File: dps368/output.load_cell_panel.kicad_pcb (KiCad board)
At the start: 2 copper layers, 50 x 46 mm, 167 parts, among them J1 Conn_01x05_Female, U1 DPS368XTSA1

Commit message: goddamn it
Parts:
- removed the ? at (141.1, 71.3)
- removed the ? at (156.6, 90.1)
- removed the ? at (134.6, 90.1)
- removed the ? at (131.3, 85.9)
- removed the ? at (131.3, 95.9)
- removed the ? at (134.6, 100.1)
- removed the ? at (142.3, 95.9)
- removed the ? at (145.6, 100.1)
- removed the ? at (142.3, 85.9)
- removed the ? at (145.6, 90.1)
- removed the ? at (141.1, 101.3)
- removed the ? at (136.7, 74.7)
- removed the ? at (136.7, 104.7)
- removed the ? at (152.1, 101.3)
- removed the ? at (147.7, 104.7)
- removed the ? at (158.7, 104.7)
- removed the ? at (163.1, 101.3)
- removed the ? at (164.3, 95.9)
- removed the ? at (167.6, 100.1)
- removed the ? at (164.3, 85.9)
- removed the ? at (167.6, 90.1)
- removed the ? at (164.3, 75.9)
- removed the ? at (152.1, 71.3)
- removed the ? at (167.6, 80.1)
- removed the ? at (153.3, 75.9)
- removed the ? at (156.6, 80.1)
- removed the ? at (145.6, 80.1)
- removed the ? at (142.3, 75.9)
- removed the ? at (131.3, 75.9)
- removed the ? at (134.6, 80.1)
- removed the ? at (130.1, 71.3)
- removed the ? at (158.7, 94.7)
- removed the ? at (163.1, 91.3)
- removed the ? at (147.7, 74.7)
- removed the ? at (147.7, 94.7)
- removed the ? at (152.1, 91.3)
- removed the ? at (136.7, 94.7)
- removed the ? at (141.1, 91.3)
- removed the ? at (141.1, 81.3)
- removed the ? at (136.7, 84.7)
- removed the ? at (152.1, 81.3)
- removed the ? at (147.7, 84.7)
- removed the ? at (163.1, 81.3)
- removed the ? at (158.7, 84.7)
- removed the ? at (163.1, 71.3)
- removed the ? at (169.7, 84.7)
- removed the ? at (169.7, 94.7)
- removed the ? at (169.7, 104.7)
- removed the ? at (164.3, 105.9)
- removed the ? at (153.3, 105.9)
- removed the ? at (142.3, 105.9)
- removed the ? at (131.3, 105.9)
- removed the ? at (130.1, 101.3)
- removed the ? at (130.1, 91.3)
- removed the ? at (130.1, 81.3)
- removed the ? at (158.7, 74.7)
- removed the ? at (134.6, 70.1)
- removed the ? at (145.6, 70.1)
- removed the ? at (156.6, 70.1)
- removed the ? at (167.6, 70.1)
- removed the ? at (169.7, 74.7)
- removed the ? at (153.3, 95.9)
- removed the ? at (156.6, 100.1)
- removed the ? at (153.3, 85.9)
- removed the C1 at (164.3, 101.3)
- removed the C1 at (153.3, 81.3)
- removed the C1 at (142.3, 81.3)
- removed the C1 at (131.3, 81.3)
- removed the C1 at (164.3, 71.3)
- removed the C1 at (153.3, 71.3)
- removed the C1 at (142.3, 71.3)
- removed the C1 at (153.3, 101.3)
- removed the C1 at (142.3, 101.3)
- removed the C1 at (131.3, 101.3)
- removed the C1 at (164.3, 91.3)
- removed the C1 at (153.3, 91.3)
- removed the C1 at (142.3, 91.3)
- removed the C1 at (131.3, 91.3)
- removed the C1 at (164.3, 81.3)
- removed the C2 at (164.3, 103.3)
- removed the C2 at (153.3, 83.3)
- removed the C2 at (142.3, 83.3)
- removed the C2 at (131.3, 83.3)
- removed the C2 at (164.3, 73.3)
- removed the C2 at (153.3, 73.3)
- removed the C2 at (142.3, 73.3)
- removed the C2 at (153.3, 103.3)
- removed the C2 at (142.3, 103.3)
- removed the C2 at (131.3, 103.3)
- removed the C2 at (164.3, 93.3)
- removed the C2 at (153.3, 93.3)
- removed the C2 at (142.3, 93.3)
- removed the C2 at (131.3, 93.3)
- removed the C2 at (164.3, 83.3)
- removed FID1, FID2, FID3: Fiducial_0.5mm_Dia_1mm_Outer, Fiducial:Fiducial_0.5mm_Dia_1mm_Outer
- removed the J1 at (163.9, 105.1)
- removed the J1 at (152.9, 85.1)
- removed the J1 at (141.9, 85.1)
- removed the J1 at (130.9, 85.1)
- removed the J1 at (163.9, 75.1)
- removed the J1 at (152.9, 75.1)
- removed the J1 at (141.9, 75.1)
- removed the J1 at (152.9, 105.1)
- removed the J1 at (141.9, 105.1)
- removed the J1 at (130.9, 105.1)
- removed the J1 at (163.9, 95.1)
- removed the J1 at (152.9, 95.1)
- removed the J1 at (141.9, 95.1)
- removed the J1 at (130.9, 95.1)
- removed the J1 at (163.9, 85.1)
- removed the R1 at (168.3, 103.3)
- removed the R1 at (157.3, 83.3)
- removed the R1 at (146.3, 83.3)
- removed the R1 at (135.3, 83.3)
- removed the R1 at (168.3, 73.3)
- removed the R1 at (157.3, 73.3)
- removed the R1 at (146.3, 73.3)
- removed the R1 at (157.3, 103.3)
- removed the R1 at (146.3, 103.3)
- removed the R1 at (135.3, 103.3)
- removed the R1 at (168.3, 93.3)
- removed the R1 at (157.3, 93.3)
- removed the R1 at (146.3, 93.3)
- removed the R1 at (135.3, 93.3)
- removed the R1 at (168.3, 83.3)
- removed the R2 at (168.3, 101.3)
- removed the R2 at (157.3, 81.3)
- removed the R2 at (146.3, 81.3)
- removed the R2 at (135.3, 81.3)
- removed the R2 at (168.3, 71.3)
- removed the R2 at (157.3, 71.3)
- removed the R2 at (146.3, 71.3)
- removed the R2 at (157.3, 101.3)
- removed the R2 at (146.3, 101.3)
- removed the R2 at (135.3, 101.3)
- removed the R2 at (168.3, 91.3)
- removed the R2 at (157.3, 91.3)
- removed the R2 at (146.3, 91.3)
- removed the R2 at (135.3, 91.3)
- removed the R2 at (168.3, 81.3)
- removed the U1 at (166.3, 101.8)
- removed the U1 at (155.3, 81.8)
- removed the U1 at (144.3, 81.8)
- removed the U1 at (133.3, 81.8)
- removed the U1 at (166.3, 71.8)
- removed the U1 at (155.3, 71.8)
- removed the U1 at (144.3, 71.8)
- removed the U1 at (155.3, 101.8)
- removed the U1 at (144.3, 101.8)
- removed the U1 at (133.3, 101.8)
- removed the U1 at (166.3, 91.8)
- removed the U1 at (155.3, 91.8)
- removed the U1 at (144.3, 91.8)
- removed the U1 at (133.3, 91.8)
- removed the U1 at (166.3, 81.8)
- added ?: , holes, F.Cu at (140.7, 72.1)
- added ?: , holes, F.Cu at (155.9, 89.5)
- added ?: , holes, F.Cu at (133.9, 89.5)
- added ?: , holes, F.Cu at (132.1, 85.5)
- added ?: , holes, F.Cu at (132.1, 95.5)
- added ?: , holes, F.Cu at (133.9, 99.5)
- added ?: , holes, F.Cu at (143.1, 95.5)
- added ?: , holes, F.Cu at (144.9, 99.5)
- added ?: , holes, F.Cu at (143.1, 85.5)
- added ?: , holes, F.Cu at (144.9, 89.5)
- added ?: , holes, F.Cu at (140.7, 102.1)
- added ?: , holes, F.Cu at (136.5, 73.9)
- added ?: , holes, F.Cu at (136.5, 103.9)
- added ?: , holes, F.Cu at (151.7, 102.1)
- added ?: , holes, F.Cu at (147.5, 103.9)
- added ?: , holes, F.Cu at (158.5, 103.9)
- added ?: , holes, F.Cu at (162.7, 102.1)
- added ?: , holes, F.Cu at (165.1, 95.5)
- added ?: , holes, F.Cu at (166.9, 99.5)
- added ?: , holes, F.Cu at (165.1, 85.5)
- added ?: , holes, F.Cu at (166.9, 89.5)
- added ?: , holes, F.Cu at (165.1, 75.5)
- added ?: , holes, F.Cu at (151.7, 72.1)
- added ?: , holes, F.Cu at (166.9, 79.5)
- added ?: , holes, F.Cu at (154.1, 75.5)
- added ?: , holes, F.Cu at (155.9, 79.5)
- added ?: , holes, F.Cu at (144.9, 79.5)
- added ?: , holes, F.Cu at (143.1, 75.5)
- added ?: , holes, F.Cu at (132.1, 75.5)
- added ?: , holes, F.Cu at (133.9, 79.5)
- added ?: , holes, F.Cu at (129.7, 72.1)
- added ?: , holes, F.Cu at (158.5, 93.9)
- added ?: , holes, F.Cu at (162.7, 92.1)
- added ?: , holes, F.Cu at (147.5, 73.9)
- added ?: , holes, F.Cu at (147.5, 93.9)
- added ?: , holes, F.Cu at (151.7, 92.1)
- added ?: , holes, F.Cu at (136.5, 93.9)
- added ?: , holes, F.Cu at (140.7, 92.1)
- added ?: , holes, F.Cu at (140.7, 82.1)
- added ?: , holes, F.Cu at (136.5, 83.9)
- added ?: , holes, F.Cu at (151.7, 82.1)
- added ?: , holes, F.Cu at (147.5, 83.9)
- added ?: , holes, F.Cu at (162.7, 82.1)
- added ?: , holes, F.Cu at (158.5, 83.9)
- added ?: , holes, F.Cu at (162.7, 72.1)
- added ?: , holes, F.Cu at (169.5, 83.9)
- added ?: , holes, F.Cu at (169.5, 93.9)
- added ?: , holes, F.Cu at (169.5, 103.9)
- added ?: , holes, F.Cu at (165.1, 105.5)
- added ?: , holes, F.Cu at (154.1, 105.5)
- added ?: , holes, F.Cu at (143.1, 105.5)
- added ?: , holes, F.Cu at (132.1, 105.5)
- added ?: , holes, F.Cu at (129.7, 102.1)
- added ?: , holes, F.Cu at (129.7, 92.1)
- added ?: , holes, F.Cu at (129.7, 82.1)
- added ?: , holes, F.Cu at (158.5, 73.9)
- added ?: , holes, F.Cu at (133.9, 69.5)
- added ?: , holes, F.Cu at (144.9, 69.5)
- added ?: , holes, F.Cu at (155.9, 69.5)
- added ?: , holes, F.Cu at (166.9, 69.5)
- added ?: , holes, F.Cu at (169.5, 73.9)
- added ?: , holes, F.Cu at (154.1, 95.5)
- added ?: , holes, F.Cu at (155.9, 99.5)
- added ?: , holes, F.Cu at (154.1, 85.5)
- added C1: 100n, Capacitor_SMD:C_0402_1005Metric, F.Cu at (164.0, 100.8)
- added C1: 100n, Capacitor_SMD:C_0402_1005Metric, F.Cu at (153.0, 80.8)
- added C1: 100n, Capacitor_SMD:C_0402_1005Metric, F.Cu at (142.0, 80.8)
- added C1: 100n, Capacitor_SMD:C_0402_1005Metric, F.Cu at (131.0, 80.8)
- added C1: 100n, Capacitor_SMD:C_0402_1005Metric, F.Cu at (164.0, 70.8)
- added C1: 100n, Capacitor_SMD:C_0402_1005Metric, F.Cu at (153.0, 70.8)
- added C1: 100n, Capacitor_SMD:C_0402_1005Metric, F.Cu at (142.0, 70.8)
- added C1: 100n, Capacitor_SMD:C_0402_1005Metric, F.Cu at (153.0, 100.8)
- added C1: 100n, Capacitor_SMD:C_0402_1005Metric, F.Cu at (142.0, 100.8)
- added C1: 100n, Capacitor_SMD:C_0402_1005Metric, F.Cu at (131.0, 100.8)
- added C1: 100n, Capacitor_SMD:C_0402_1005Metric, F.Cu at (164.0, 90.8)
- added C1: 100n, Capacitor_SMD:C_0402_1005Metric, F.Cu at (153.0, 90.8)
- added C1: 100n, Capacitor_SMD:C_0402_1005Metric, F.Cu at (142.0, 90.8)
- added C1: 100n, Capacitor_SMD:C_0402_1005Metric, F.Cu at (131.0, 90.8)
- added C1: 100n, Capacitor_SMD:C_0402_1005Metric, F.Cu at (164.0, 80.8)
- added C2: 100n, Capacitor_SMD:C_0402_1005Metric, F.Cu at (164.0, 102.8)
- added C2: 100n, Capacitor_SMD:C_0402_1005Metric, F.Cu at (153.0, 82.8)
- added C2: 100n, Capacitor_SMD:C_0402_1005Metric, F.Cu at (142.0, 82.8)
- added C2: 100n, Capacitor_SMD:C_0402_1005Metric, F.Cu at (131.0, 82.8)
- added C2: 100n, Capacitor_SMD:C_0402_1005Metric, F.Cu at (164.0, 72.8)
- added C2: 100n, Capacitor_SMD:C_0402_1005Metric, F.Cu at (153.0, 72.8)
- added C2: 100n, Capacitor_SMD:C_0402_1005Metric, F.Cu at (142.0, 72.8)
- added C2: 100n, Capacitor_SMD:C_0402_1005Metric, F.Cu at (153.0, 102.8)
- added C2: 100n, Capacitor_SMD:C_0402_1005Metric, F.Cu at (142.0, 102.8)
- added C2: 100n, Capacitor_SMD:C_0402_1005Metric, F.Cu at (131.0, 102.8)
- added C2: 100n, Capacitor_SMD:C_0402_1005Metric, F.Cu at (164.0, 92.8)
- added C2: 100n, Capacitor_SMD:C_0402_1005Metric, F.Cu at (153.0, 92.8)
- added C2: 100n, Capacitor_SMD:C_0402_1005Metric, F.Cu at (142.0, 92.8)
- added C2: 100n, Capacitor_SMD:C_0402_1005Metric, F.Cu at (131.0, 92.8)
- added C2: 100n, Capacitor_SMD:C_0402_1005Metric, F.Cu at (164.0, 82.8)
- added J1: Conn_01x05_Female, Connector_PinHeader_1.27mm:PinHeader_1x05_P1.27mm_Vertical, F.Cu at (163.6, 104.6)
- added J1: Conn_01x05_Female, Connector_PinHeader_1.27mm:PinHeader_1x05_P1.27mm_Vertical, F.Cu at (152.6, 84.6)
- added J1: Conn_01x05_Female, Connector_PinHeader_1.27mm:PinHeader_1x05_P1.27mm_Vertical, F.Cu at (141.6, 84.6)
- added J1: Conn_01x05_Female, Connector_PinHeader_1.27mm:PinHeader_1x05_P1.27mm_Vertical, F.Cu at (130.6, 84.6)
- added J1: Conn_01x05_Female, Connector_PinHeader_1.27mm:PinHeader_1x05_P1.27mm_Vertical, F.Cu at (163.6, 74.6)
- added J1: Conn_01x05_Female, Connector_PinHeader_1.27mm:PinHeader_1x05_P1.27mm_Vertical, F.Cu at (152.6, 74.6)
- added J1: Conn_01x05_Female, Connector_PinHeader_1.27mm:PinHeader_1x05_P1.27mm_Vertical, F.Cu at (141.6, 74.6)
- added J1: Conn_01x05_Female, Connector_PinHeader_1.27mm:PinHeader_1x05_P1.27mm_Vertical, F.Cu at (152.6, 104.6)
- added J1: Conn_01x05_Female, Connector_PinHeader_1.27mm:PinHeader_1x05_P1.27mm_Vertical, F.Cu at (141.6, 104.6)
- added J1: Conn_01x05_Female, Connector_PinHeader_1.27mm:PinHeader_1x05_P1.27mm_Vertical, F.Cu at (130.6, 104.6)
- added J1: Conn_01x05_Female, Connector_PinHeader_1.27mm:PinHeader_1x05_P1.27mm_Vertical, F.Cu at (163.6, 94.6)
- added J1: Conn_01x05_Female, Connector_PinHeader_1.27mm:PinHeader_1x05_P1.27mm_Vertical, F.Cu at (152.6, 94.6)
- added J1: Conn_01x05_Female, Connector_PinHeader_1.27mm:PinHeader_1x05_P1.27mm_Vertical, F.Cu at (141.6, 94.6)
- added J1: Conn_01x05_Female, Connector_PinHeader_1.27mm:PinHeader_1x05_P1.27mm_Vertical, F.Cu at (130.6, 94.6)
- added J1: Conn_01x05_Female, Connector_PinHeader_1.27mm:PinHeader_1x05_P1.27mm_Vertical, F.Cu at (163.6, 84.6)
- added R1: 10k, Resistor_SMD:R_0402_1005Metric, F.Cu at (168.0, 102.8)
- added R1: 10k, Resistor_SMD:R_0402_1005Metric, F.Cu at (157.0, 82.8)
- added R1: 10k, Resistor_SMD:R_0402_1005Metric, F.Cu at (146.0, 82.8)
- added R1: 10k, Resistor_SMD:R_0402_1005Metric, F.Cu at (135.0, 82.8)
- added R1: 10k, Resistor_SMD:R_0402_1005Metric, F.Cu at (168.0, 72.8)
- added R1: 10k, Resistor_SMD:R_0402_1005Metric, F.Cu at (157.0, 72.8)
- added R1: 10k, Resistor_SMD:R_0402_1005Metric, F.Cu at (146.0, 72.8)
- added R1: 10k, Resistor_SMD:R_0402_1005Metric, F.Cu at (157.0, 102.8)
- added R1: 10k, Resistor_SMD:R_0402_1005Metric, F.Cu at (146.0, 102.8)
- added R1: 10k, Resistor_SMD:R_0402_1005Metric, F.Cu at (135.0, 102.8)
- added R1: 10k, Resistor_SMD:R_0402_1005Metric, F.Cu at (168.0, 92.8)
- added R1: 10k, Resistor_SMD:R_0402_1005Metric, F.Cu at (157.0, 92.8)
- added R1: 10k, Resistor_SMD:R_0402_1005Metric, F.Cu at (146.0, 92.8)
- added R1: 10k, Resistor_SMD:R_0402_1005Metric, F.Cu at (135.0, 92.8)
- added R1: 10k, Resistor_SMD:R_0402_1005Metric, F.Cu at (168.0, 82.8)
- added R2: 10k, Resistor_SMD:R_0402_1005Metric, F.Cu at (168.0, 100.8)
- added R2: 10k, Resistor_SMD:R_0402_1005Metric, F.Cu at (157.0, 80.8)
- added R2: 10k, Resistor_SMD:R_0402_1005Metric, F.Cu at (146.0, 80.8)
- added R2: 10k, Resistor_SMD:R_0402_1005Metric, F.Cu at (135.0, 80.8)
- added R2: 10k, Resistor_SMD:R_0402_1005Metric, F.Cu at (168.0, 70.8)
- added R2: 10k, Resistor_SMD:R_0402_1005Metric, F.Cu at (157.0, 70.8)
- added R2: 10k, Resistor_SMD:R_0402_1005Metric, F.Cu at (146.0, 70.8)
- added R2: 10k, Resistor_SMD:R_0402_1005Metric, F.Cu at (157.0, 100.8)
- added R2: 10k, Resistor_SMD:R_0402_1005Metric, F.Cu at (146.0, 100.8)
- added R2: 10k, Resistor_SMD:R_0402_1005Metric, F.Cu at (135.0, 100.8)
- added R2: 10k, Resistor_SMD:R_0402_1005Metric, F.Cu at (168.0, 90.8)
- added R2: 10k, Resistor_SMD:R_0402_1005Metric, F.Cu at (157.0, 90.8)
- added R2: 10k, Resistor_SMD:R_0402_1005Metric, F.Cu at (146.0, 90.8)
- added R2: 10k, Resistor_SMD:R_0402_1005Metric, F.Cu at (135.0, 90.8)
- added R2: 10k, Resistor_SMD:R_0402_1005Metric, F.Cu at (168.0, 80.8)
- added U1: DPS368XTSA1, custom_lib:XDCR_DPS368XTSA1, F.Cu at (166.0, 101.3)
- added U1: DPS368XTSA1, custom_lib:XDCR_DPS368XTSA1, F.Cu at (155.0, 81.3)
- added U1: DPS368XTSA1, custom_lib:XDCR_DPS368XTSA1, F.Cu at (144.0, 81.3)
- added U1: DPS368XTSA1, custom_lib:XDCR_DPS368XTSA1, F.Cu at (133.0, 81.3)
- added U1: DPS368XTSA1, custom_lib:XDCR_DPS368XTSA1, F.Cu at (166.0, 71.3)
- added U1: DPS368XTSA1, custom_lib:XDCR_DPS368XTSA1, F.Cu at (155.0, 71.3)
- added U1: DPS368XTSA1, custom_lib:XDCR_DPS368XTSA1, F.Cu at (144.0, 71.3)
- added U1: DPS368XTSA1, custom_lib:XDCR_DPS368XTSA1, F.Cu at (155.0, 101.3)
- added U1: DPS368XTSA1, custom_lib:XDCR_DPS368XTSA1, F.Cu at (144.0, 101.3)
- added U1: DPS368XTSA1, custom_lib:XDCR_DPS368XTSA1, F.Cu at (133.0, 101.3)
- added U1: DPS368XTSA1, custom_lib:XDCR_DPS368XTSA1, F.Cu at (166.0, 91.3)
- added U1: DPS368XTSA1, custom_lib:XDCR_DPS368XTSA1, F.Cu at (155.0, 91.3)
- added U1: DPS368XTSA1, custom_lib:XDCR_DPS368XTSA1, F.Cu at (144.0, 91.3)
- added U1: DPS368XTSA1, custom_lib:XDCR_DPS368XTSA1, F.Cu at (133.0, 91.3)
- added U1: DPS368XTSA1, custom_lib:XDCR_DPS368XTSA1, F.Cu at (166.0, 81.3)
- moved C1 0.58 mm to (131.0, 70.8)
- moved C2 0.58 mm to (131.0, 72.8)
- moved J1 0.58 mm to (130.6, 74.6)
- moved R1 0.58 mm to (135.0, 72.8)
- moved R2 0.58 mm to (135.0, 70.8)
- moved U1 0.58 mm to (133.0, 71.3)
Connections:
- C1 pad 1: +3V3 -> GND
- C1 pad 2: Net-(C1-Pad2) -> +3V3
- C2 pad 1: Net-(C2-Pad1) -> GND
- U1 pad 6: Net-(C2-Pad1) -> +3V3
- U1 pad 8: Net-(C1-Pad2) -> +3V3
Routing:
- net +3V3: track 172.3 -> 235.8 mm
- net GND: track 107.3 -> 153.3 mm
- net Net-(C2-Pad1): track 42.5 -> 0.00 mm
- net Net-(C1-Pad2): track 20.6 -> 0.00 mm
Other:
- outline, holes or cut-outs redrawn

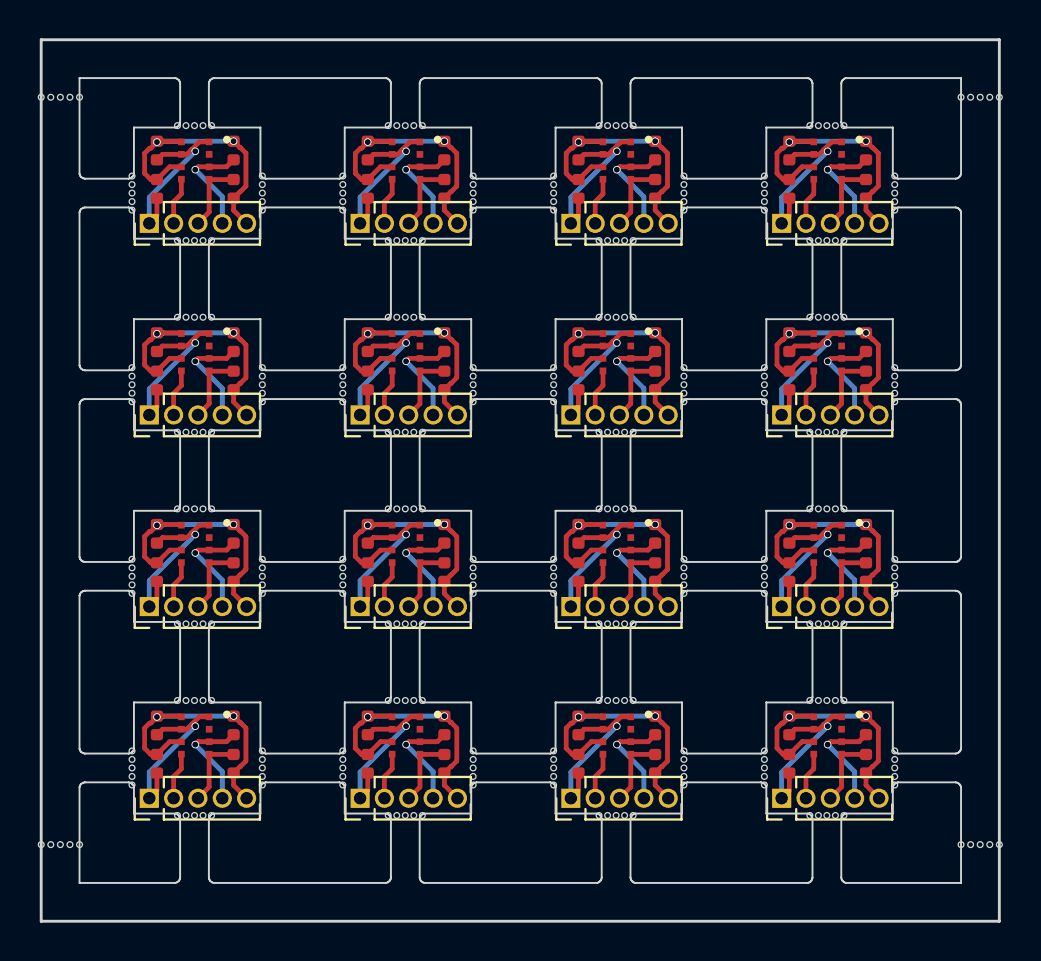
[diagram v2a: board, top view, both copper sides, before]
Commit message: 7mm diameter sensor
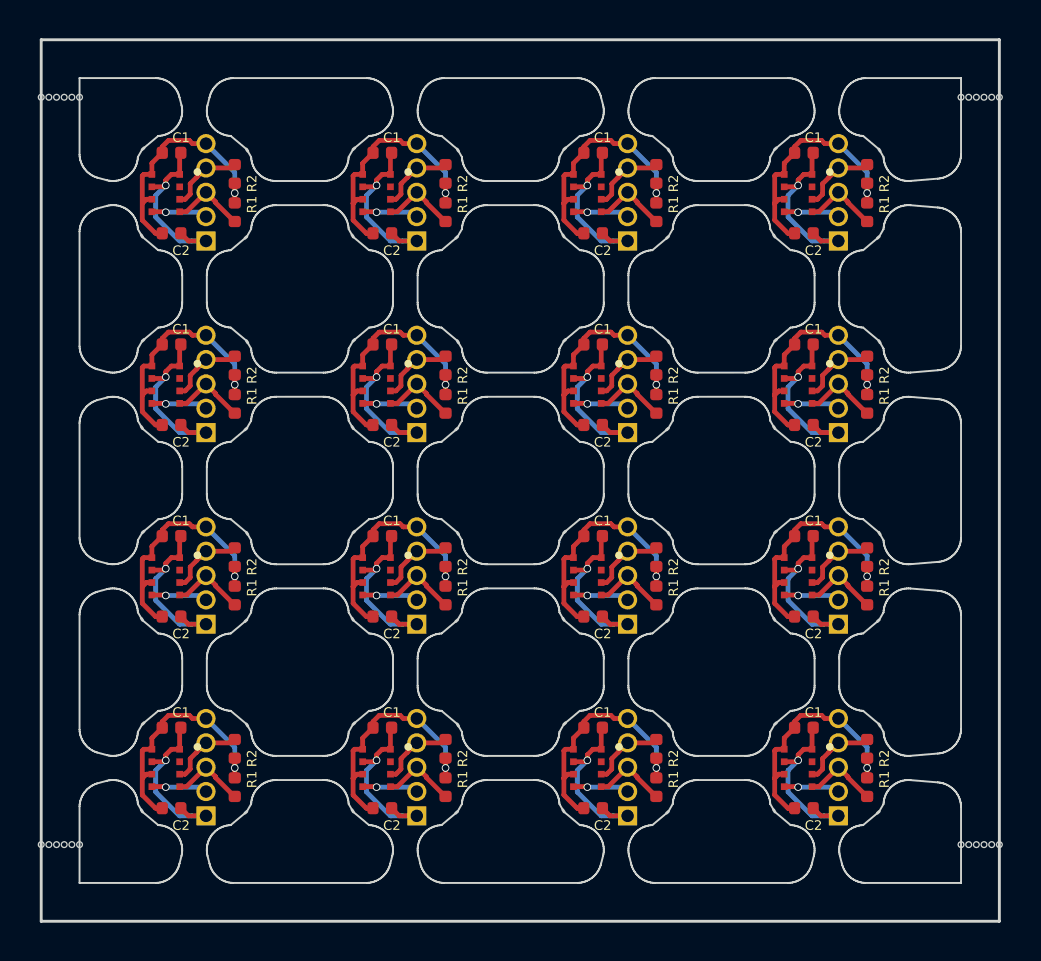
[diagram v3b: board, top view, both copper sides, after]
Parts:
- removed the ? at (140.7, 72.1)
- removed the ? at (155.9, 89.5)
- removed the ? at (133.9, 89.5)
- removed the ? at (132.1, 85.5)
- removed the ? at (132.1, 95.5)
- removed the ? at (133.9, 99.5)
- removed the ? at (143.1, 95.5)
- removed the ? at (144.9, 99.5)
- removed the ? at (143.1, 85.5)
- removed the ? at (144.9, 89.5)
- removed the ? at (140.7, 102.1)
- removed the ? at (136.5, 73.9)
- removed the ? at (136.5, 103.9)
- removed the ? at (151.7, 102.1)
- removed the ? at (147.5, 103.9)
- removed the ? at (158.5, 103.9)
- removed the ? at (162.7, 102.1)
- removed the ? at (165.1, 95.5)
- removed the ? at (166.9, 99.5)
- removed the ? at (165.1, 85.5)
- removed the ? at (166.9, 89.5)
- removed the ? at (165.1, 75.5)
- removed the ? at (151.7, 72.1)
- removed the ? at (166.9, 79.5)
- removed the ? at (154.1, 75.5)
- removed the ? at (155.9, 79.5)
- removed the ? at (144.9, 79.5)
- removed the ? at (143.1, 75.5)
- removed the ? at (132.1, 75.5)
- removed the ? at (133.9, 79.5)
- removed the ? at (129.7, 72.1)
- removed the ? at (158.5, 93.9)
- removed the ? at (162.7, 92.1)
- removed the ? at (147.5, 73.9)
- removed the ? at (147.5, 93.9)
- removed the ? at (151.7, 92.1)
- removed the ? at (136.5, 93.9)
- removed the ? at (140.7, 92.1)
- removed the ? at (140.7, 82.1)
- removed the ? at (136.5, 83.9)
- removed the ? at (151.7, 82.1)
- removed the ? at (147.5, 83.9)
- removed the ? at (162.7, 82.1)
- removed the ? at (158.5, 83.9)
- removed the ? at (162.7, 72.1)
- removed the ? at (169.5, 83.9)
- removed the ? at (169.5, 93.9)
- removed the ? at (169.5, 103.9)
- removed the ? at (165.1, 105.5)
- removed the ? at (154.1, 105.5)
- removed the ? at (143.1, 105.5)
- removed the ? at (132.1, 105.5)
- removed the ? at (129.7, 102.1)
- removed the ? at (129.7, 92.1)
- removed the ? at (129.7, 82.1)
- removed the ? at (158.5, 73.9)
- removed the ? at (133.9, 69.5)
- removed the ? at (144.9, 69.5)
- removed the ? at (155.9, 69.5)
- removed the ? at (166.9, 69.5)
- removed the ? at (169.5, 73.9)
- removed the ? at (154.1, 95.5)
- removed the ? at (155.9, 99.5)
- removed the ? at (154.1, 85.5)
- removed the C1 at (164.0, 100.8)
- removed the C1 at (153.0, 80.8)
- removed the C1 at (142.0, 80.8)
- removed the C1 at (131.0, 80.8)
- removed the C1 at (164.0, 70.8)
- removed the C1 at (153.0, 70.8)
- removed the C1 at (142.0, 70.8)
- removed the C1 at (153.0, 100.8)
- removed the C1 at (142.0, 100.8)
- removed the C1 at (131.0, 100.8)
- removed the C1 at (164.0, 90.8)
- removed the C1 at (153.0, 90.8)
- removed the C1 at (142.0, 90.8)
- removed the C1 at (131.0, 90.8)
- removed the C1 at (164.0, 80.8)
- removed the C2 at (164.0, 102.8)
- removed the C2 at (153.0, 82.8)
- removed the C2 at (142.0, 82.8)
- removed the C2 at (131.0, 82.8)
- removed the C2 at (164.0, 72.8)
- removed the C2 at (153.0, 72.8)
- removed the C2 at (142.0, 72.8)
- removed the C2 at (131.0, 72.8)
- removed the C2 at (153.0, 102.8)
- removed the C2 at (142.0, 102.8)
- removed the C2 at (131.0, 102.8)
- removed the C2 at (164.0, 92.8)
- removed the C2 at (153.0, 92.8)
- removed the C2 at (142.0, 92.8)
- removed the C2 at (131.0, 92.8)
- removed the C2 at (164.0, 82.8)
- removed the J1 at (163.6, 104.6)
- removed the J1 at (152.6, 84.6)
- removed the J1 at (141.6, 84.6)
- removed the J1 at (130.6, 84.6)
- removed the J1 at (163.6, 74.6)
- removed the J1 at (152.6, 74.6)
- removed the J1 at (141.6, 74.6)
- removed the J1 at (152.6, 104.6)
- removed the J1 at (141.6, 104.6)
- removed the J1 at (130.6, 104.6)
- removed the J1 at (163.6, 94.6)
- removed the J1 at (152.6, 94.6)
- removed the J1 at (141.6, 94.6)
- removed the J1 at (130.6, 94.6)
- removed the J1 at (163.6, 84.6)
- removed the R1 at (168.0, 102.8)
- removed the R1 at (157.0, 82.8)
- removed the R1 at (146.0, 82.8)
- removed the R1 at (135.0, 82.8)
- removed the R1 at (168.0, 72.8)
- removed the R1 at (157.0, 72.8)
- removed the R1 at (146.0, 72.8)
- removed the R1 at (157.0, 102.8)
- removed the R1 at (146.0, 102.8)
- removed the R1 at (135.0, 102.8)
- removed the R1 at (168.0, 92.8)
- removed the R1 at (157.0, 92.8)
- removed the R1 at (146.0, 92.8)
- removed the R1 at (135.0, 92.8)
- removed the R1 at (168.0, 82.8)
- removed the R2 at (168.0, 100.8)
- removed the R2 at (157.0, 80.8)
- removed the R2 at (146.0, 80.8)
- removed the R2 at (135.0, 80.8)
- removed the R2 at (168.0, 70.8)
- removed the R2 at (157.0, 70.8)
- removed the R2 at (146.0, 70.8)
- removed the R2 at (135.0, 70.8)
- removed the R2 at (157.0, 100.8)
- removed the R2 at (146.0, 100.8)
- removed the R2 at (135.0, 100.8)
- removed the R2 at (168.0, 90.8)
- removed the R2 at (157.0, 90.8)
- removed the R2 at (146.0, 90.8)
- removed the R2 at (135.0, 90.8)
- removed the R2 at (168.0, 80.8)
- removed the U1 at (166.0, 101.3)
- removed the U1 at (155.0, 81.3)
- removed the U1 at (144.0, 81.3)
- removed the U1 at (133.0, 81.3)
- removed the U1 at (166.0, 71.3)
- removed the U1 at (155.0, 71.3)
- removed the U1 at (144.0, 71.3)
- removed the U1 at (133.0, 71.3)
- removed the U1 at (155.0, 101.3)
- removed the U1 at (144.0, 101.3)
- removed the U1 at (133.0, 101.3)
- removed the U1 at (166.0, 91.3)
- removed the U1 at (155.0, 91.3)
- removed the U1 at (144.0, 91.3)
- removed the U1 at (133.0, 91.3)
- removed the U1 at (166.0, 81.3)
- added C1: 100n, Capacitor_SMD:C_0402_1005Metric, F.Cu at (164.8, 70.9)
- added C1: 100n, Capacitor_SMD:C_0402_1005Metric, F.Cu at (164.8, 80.9)
- added C1: 100n, Capacitor_SMD:C_0402_1005Metric, F.Cu at (153.8, 70.9)
- added C1: 100n, Capacitor_SMD:C_0402_1005Metric, F.Cu at (142.8, 100.9)
- added C1: 100n, Capacitor_SMD:C_0402_1005Metric, F.Cu at (131.8, 90.9)
- added C1: 100n, Capacitor_SMD:C_0402_1005Metric, F.Cu at (131.8, 100.9)
- added C1: 100n, Capacitor_SMD:C_0402_1005Metric, F.Cu at (131.8, 80.9)
- added C1: 100n, Capacitor_SMD:C_0402_1005Metric, F.Cu at (142.8, 90.9)
- added C1: 100n, Capacitor_SMD:C_0402_1005Metric, F.Cu at (153.8, 100.9)
- added C1: 100n, Capacitor_SMD:C_0402_1005Metric, F.Cu at (153.8, 90.9)
- added C1: 100n, Capacitor_SMD:C_0402_1005Metric, F.Cu at (164.8, 100.9)
- added C1: 100n, Capacitor_SMD:C_0402_1005Metric, F.Cu at (153.8, 80.9)
- added C1: 100n, Capacitor_SMD:C_0402_1005Metric, F.Cu at (164.8, 90.9)
- added C1: 100n, Capacitor_SMD:C_0402_1005Metric, F.Cu at (142.8, 70.9)
- added C1: 100n, Capacitor_SMD:C_0402_1005Metric, F.Cu at (142.8, 80.9)
- added C2: 100n, Capacitor_SMD:C_0402_1005Metric, F.Cu at (164.8, 95.1)
- added C2: 100n, Capacitor_SMD:C_0402_1005Metric, F.Cu at (153.8, 75.1)
- added C2: 100n, Capacitor_SMD:C_0402_1005Metric, F.Cu at (164.8, 105.1)
- added C2: 100n, Capacitor_SMD:C_0402_1005Metric, F.Cu at (164.8, 85.1)
- added C2: 100n, Capacitor_SMD:C_0402_1005Metric, F.Cu at (131.8, 105.1)
- added C2: 100n, Capacitor_SMD:C_0402_1005Metric, F.Cu at (131.8, 85.1)
- added C2: 100n, Capacitor_SMD:C_0402_1005Metric, F.Cu at (131.8, 95.1)
- added C2: 100n, Capacitor_SMD:C_0402_1005Metric, F.Cu at (131.8, 75.1)
- added C2: 100n, Capacitor_SMD:C_0402_1005Metric, F.Cu at (153.8, 95.1)
- added C2: 100n, Capacitor_SMD:C_0402_1005Metric, F.Cu at (142.8, 95.1)
- added C2: 100n, Capacitor_SMD:C_0402_1005Metric, F.Cu at (153.8, 105.1)
- added C2: 100n, Capacitor_SMD:C_0402_1005Metric, F.Cu at (142.8, 105.1)
- added C2: 100n, Capacitor_SMD:C_0402_1005Metric, F.Cu at (142.8, 75.1)
- added C2: 100n, Capacitor_SMD:C_0402_1005Metric, F.Cu at (153.8, 85.1)
- added C2: 100n, Capacitor_SMD:C_0402_1005Metric, F.Cu at (164.8, 75.1)
- added C2: 100n, Capacitor_SMD:C_0402_1005Metric, F.Cu at (142.8, 85.1)
- added J1: Conn_01x05_Female, Connector_PinHeader_1.27mm:PinHeader_1x05_P1.27mm_Vertical, B.Cu at (166.6, 95.5)
- added J1: Conn_01x05_Female, Connector_PinHeader_1.27mm:PinHeader_1x05_P1.27mm_Vertical, B.Cu at (155.6, 75.5)
- added J1: Conn_01x05_Female, Connector_PinHeader_1.27mm:PinHeader_1x05_P1.27mm_Vertical, B.Cu at (144.6, 75.5)
- added J1: Conn_01x05_Female, Connector_PinHeader_1.27mm:PinHeader_1x05_P1.27mm_Vertical, B.Cu at (166.6, 105.5)
- added J1: Conn_01x05_Female, Connector_PinHeader_1.27mm:PinHeader_1x05_P1.27mm_Vertical, B.Cu at (133.6, 105.5)
- added J1: Conn_01x05_Female, Connector_PinHeader_1.27mm:PinHeader_1x05_P1.27mm_Vertical, B.Cu at (133.6, 95.5)
- added J1: Conn_01x05_Female, Connector_PinHeader_1.27mm:PinHeader_1x05_P1.27mm_Vertical, B.Cu at (133.6, 85.5)
- added J1: Conn_01x05_Female, Connector_PinHeader_1.27mm:PinHeader_1x05_P1.27mm_Vertical, B.Cu at (155.6, 105.5)
- added J1: Conn_01x05_Female, Connector_PinHeader_1.27mm:PinHeader_1x05_P1.27mm_Vertical, B.Cu at (144.6, 105.5)
- added J1: Conn_01x05_Female, Connector_PinHeader_1.27mm:PinHeader_1x05_P1.27mm_Vertical, B.Cu at (155.6, 95.5)
- added J1: Conn_01x05_Female, Connector_PinHeader_1.27mm:PinHeader_1x05_P1.27mm_Vertical, B.Cu at (144.6, 95.5)
- added J1: Conn_01x05_Female, Connector_PinHeader_1.27mm:PinHeader_1x05_P1.27mm_Vertical, B.Cu at (166.6, 85.5)
- added J1: Conn_01x05_Female, Connector_PinHeader_1.27mm:PinHeader_1x05_P1.27mm_Vertical, B.Cu at (155.6, 85.5)
- added J1: Conn_01x05_Female, Connector_PinHeader_1.27mm:PinHeader_1x05_P1.27mm_Vertical, B.Cu at (144.6, 85.5)
- added J1: Conn_01x05_Female, Connector_PinHeader_1.27mm:PinHeader_1x05_P1.27mm_Vertical, B.Cu at (166.6, 75.5)
- added R1: 10k, Resistor_SMD:R_0402_1005Metric, F.Cu at (168.1, 74.0)
- added R1: 10k, Resistor_SMD:R_0402_1005Metric, F.Cu at (157.1, 84.0)
- added R1: 10k, Resistor_SMD:R_0402_1005Metric, F.Cu at (157.1, 74.0)
- added R1: 10k, Resistor_SMD:R_0402_1005Metric, F.Cu at (168.1, 84.0)
- added R1: 10k, Resistor_SMD:R_0402_1005Metric, F.Cu at (135.1, 104.0)
- added R1: 10k, Resistor_SMD:R_0402_1005Metric, F.Cu at (135.1, 84.0)
- added R1: 10k, Resistor_SMD:R_0402_1005Metric, F.Cu at (135.1, 94.0)
- added R1: 10k, Resistor_SMD:R_0402_1005Metric, F.Cu at (146.1, 94.0)
- added R1: 10k, Resistor_SMD:R_0402_1005Metric, F.Cu at (157.1, 94.0)
- added R1: 10k, Resistor_SMD:R_0402_1005Metric, F.Cu at (168.1, 94.0)
- added R1: 10k, Resistor_SMD:R_0402_1005Metric, F.Cu at (146.1, 84.0)
- added R1: 10k, Resistor_SMD:R_0402_1005Metric, F.Cu at (146.1, 74.0)
- added R1: 10k, Resistor_SMD:R_0402_1005Metric, F.Cu at (146.1, 104.0)
- added R1: 10k, Resistor_SMD:R_0402_1005Metric, F.Cu at (157.1, 104.0)
- added R1: 10k, Resistor_SMD:R_0402_1005Metric, F.Cu at (168.1, 104.0)
- added R2: 10k, Resistor_SMD:R_0402_1005Metric, F.Cu at (168.1, 92.0)
- added R2: 10k, Resistor_SMD:R_0402_1005Metric, F.Cu at (168.1, 102.0)
- added R2: 10k, Resistor_SMD:R_0402_1005Metric, F.Cu at (157.1, 72.0)
- added R2: 10k, Resistor_SMD:R_0402_1005Metric, F.Cu at (146.1, 72.0)
- added R2: 10k, Resistor_SMD:R_0402_1005Metric, F.Cu at (135.1, 82.0)
- added R2: 10k, Resistor_SMD:R_0402_1005Metric, F.Cu at (135.1, 102.0)
- added R2: 10k, Resistor_SMD:R_0402_1005Metric, F.Cu at (135.1, 92.0)
- added R2: 10k, Resistor_SMD:R_0402_1005Metric, F.Cu at (135.1, 72.0)
- added R2: 10k, Resistor_SMD:R_0402_1005Metric, F.Cu at (157.1, 92.0)
- added R2: 10k, Resistor_SMD:R_0402_1005Metric, F.Cu at (146.1, 92.0)
- added R2: 10k, Resistor_SMD:R_0402_1005Metric, F.Cu at (168.1, 72.0)
- added R2: 10k, Resistor_SMD:R_0402_1005Metric, F.Cu at (157.1, 102.0)
- added R2: 10k, Resistor_SMD:R_0402_1005Metric, F.Cu at (146.1, 102.0)
- added R2: 10k, Resistor_SMD:R_0402_1005Metric, F.Cu at (146.1, 82.0)
- added R2: 10k, Resistor_SMD:R_0402_1005Metric, F.Cu at (168.1, 82.0)
- added R2: 10k, Resistor_SMD:R_0402_1005Metric, F.Cu at (157.1, 82.0)
- added U1: DPS368XTSA1, custom_lib:XDCR_DPS368XTSA1, F.Cu at (164.5, 93.0)
- added U1: DPS368XTSA1, custom_lib:XDCR_DPS368XTSA1, F.Cu at (153.5, 103.0)
- added U1: DPS368XTSA1, custom_lib:XDCR_DPS368XTSA1, F.Cu at (153.5, 93.0)
- added U1: DPS368XTSA1, custom_lib:XDCR_DPS368XTSA1, F.Cu at (164.5, 83.0)
- added U1: DPS368XTSA1, custom_lib:XDCR_DPS368XTSA1, F.Cu at (131.5, 93.0)
- added U1: DPS368XTSA1, custom_lib:XDCR_DPS368XTSA1, F.Cu at (131.5, 103.0)
- added U1: DPS368XTSA1, custom_lib:XDCR_DPS368XTSA1, F.Cu at (131.5, 83.0)
- added U1: DPS368XTSA1, custom_lib:XDCR_DPS368XTSA1, F.Cu at (131.5, 73.0)
- added U1: DPS368XTSA1, custom_lib:XDCR_DPS368XTSA1, F.Cu at (142.5, 83.0)
- added U1: DPS368XTSA1, custom_lib:XDCR_DPS368XTSA1, F.Cu at (164.5, 103.0)
- added U1: DPS368XTSA1, custom_lib:XDCR_DPS368XTSA1, F.Cu at (164.5, 73.0)
- added U1: DPS368XTSA1, custom_lib:XDCR_DPS368XTSA1, F.Cu at (142.5, 103.0)
- added U1: DPS368XTSA1, custom_lib:XDCR_DPS368XTSA1, F.Cu at (142.5, 93.0)
- added U1: DPS368XTSA1, custom_lib:XDCR_DPS368XTSA1, F.Cu at (153.5, 73.0)
- added U1: DPS368XTSA1, custom_lib:XDCR_DPS368XTSA1, F.Cu at (153.5, 83.0)
- added U1: DPS368XTSA1, custom_lib:XDCR_DPS368XTSA1, F.Cu at (142.5, 73.0)
- J1: moved to B.Cu
- moved J1 3.10 mm to (133.6, 75.5), turned to 0 degrees
- moved R1 1.22 mm to (135.1, 74.0), turned to 270 degrees
- moved C1 0.77 mm to (131.8, 70.9), turned to 180 degrees
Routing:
- net /sdi: track 89.6 -> 63.1 mm, vias 16 -> 0
- net +3V3: track 235.8 -> 210.3 mm, vias 32 -> 16
- net /sdo: track 39.5 -> 46.9 mm, vias 0 -> 16
- net /sck: track 61.2 -> 63.2 mm
- net GND: track 153.3 -> 152.4 mm
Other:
- outline, holes or cut-outs redrawn
- rule pad_to_mask_clearance: 0.051 -> 0.04
- rule solder_mask_min_width: 0.25 -> 0.01
- board text removed: "All"
- board text removed: "MLCC"
